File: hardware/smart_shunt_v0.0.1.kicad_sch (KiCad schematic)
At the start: 42 parts, among them J1 SHUNT +, J2 SHUNT -, J3 VIn, J4 USB_C_Receptacle_USB2.0, J5 GND, SW1 SW_Push, SW2 SW_Push, U1 ESP32-C3-MINI-1, U4 INA226, U5 TPS562201

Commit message: v0.0.2 update, before FETs
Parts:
- removed JP1: SolderJumper_2_Open, Jumper:SolderJumper-2_P1.3mm_Open_TrianglePad1.0x1.5mm, symbol Jumper:SolderJumper_2_Open
- removed TP3, TP4, TP5, TP6, TP7, TP8, TP9: TestPoint, TestPoint:TestPoint_Pad_D1.0mm, symbol Connector:TestPoint
- added D5: 1N5819WS, Diode_SMD:D_SOD-323, symbol Diode:1N5819WS
- J1, J2: footprint Acea:MountingHole_10.5mm -> ShuntToPCB:MountingHole_17mm
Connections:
- net SHUNT+: now also C4.1, C6.1, U4.8 (Vbus), U5.3 (VIN), U5.5 (EN), D5.1 (K)
- net USB_VBUS: now also D5.2 (A)
- net LOAD_DISCONNECT: now reaches U1.19 (GPIO5/ADC2_CH0)
- removed net BATTV: C4.1, C6.1, J3.1 (Pin_1), U4.8 (Vbus), U5.3 (VIN), U5.5 (EN)
- no-connect marks 8 -> 7
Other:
- note added: "Counts the current draw from the shunt"
- moved on the sheet: C10, C3, C4, C6, C7, C9, J3, J5, L1, R11, R12, U5

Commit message: v0.0.3 off to JLCPCB
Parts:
- added C11: 100nF, Capacitor_SMD:C_0603_1608Metric, symbol Device:C_Small
- added C12: 220nF, Capacitor_SMD:C_0805_2012Metric, symbol Device:C_Small
- added C13: 220uF 50V, Capacitor_SMD:CP_Elec_8x10.5, symbol Device:C_Polarized_Small
- added J6: SHUNT +, ShuntToPCB:MountingHole_17mm, symbol Connector:Conn_01x01_Socket
- added Q1, Q2: CMSL008N06, CMSL008N06:CMSL008N06, symbol Transistor_FET:STD7NK40Z
- added R13: 33.2k, Resistor_SMD:R_0603_1608Metric, symbol Device:R
- added R14: 180k, Resistor_SMD:R_0603_1608Metric, symbol Device:R
- added U2: LM74502H-Q1, Package_TO_SOT_SMD:SOT-23-8, symbol Sensor_Energy:INA219BxDCN
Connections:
- net GND: now also C11.2, C13.2, R13.2, U2.2 (GND), U2.7 (OV)
- net SHUNT+: now also C11.1, C12.1, C13.1, Q1.2 (D), Q2.2 (D), U2.5 (VS)
- net at U1.6 (GPIO3/ADC1_CH3): now also R13.1, R14.2
- net at J3.1 (Pin_1): now also R14.1
- net LOAD_DISCONNECT renamed LD_DISC
- net LD_DISC: now also U2.1 (EN)
- new net: J6.1 (Pin_1), Q1.3 (S), Q2.3 (S), U2.8 (SRC)
- new net GATE: Q1.1 (G), Q2.1 (G), U2.6 (GATE)
- new net VCAP: C12.2, U2.4 (VCAP)
- no-connect marks 7 -> 6
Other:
- moved on the sheet: C1, C10, C2, C3, C4, C5, C6, C7, C8, C9, D1, D5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

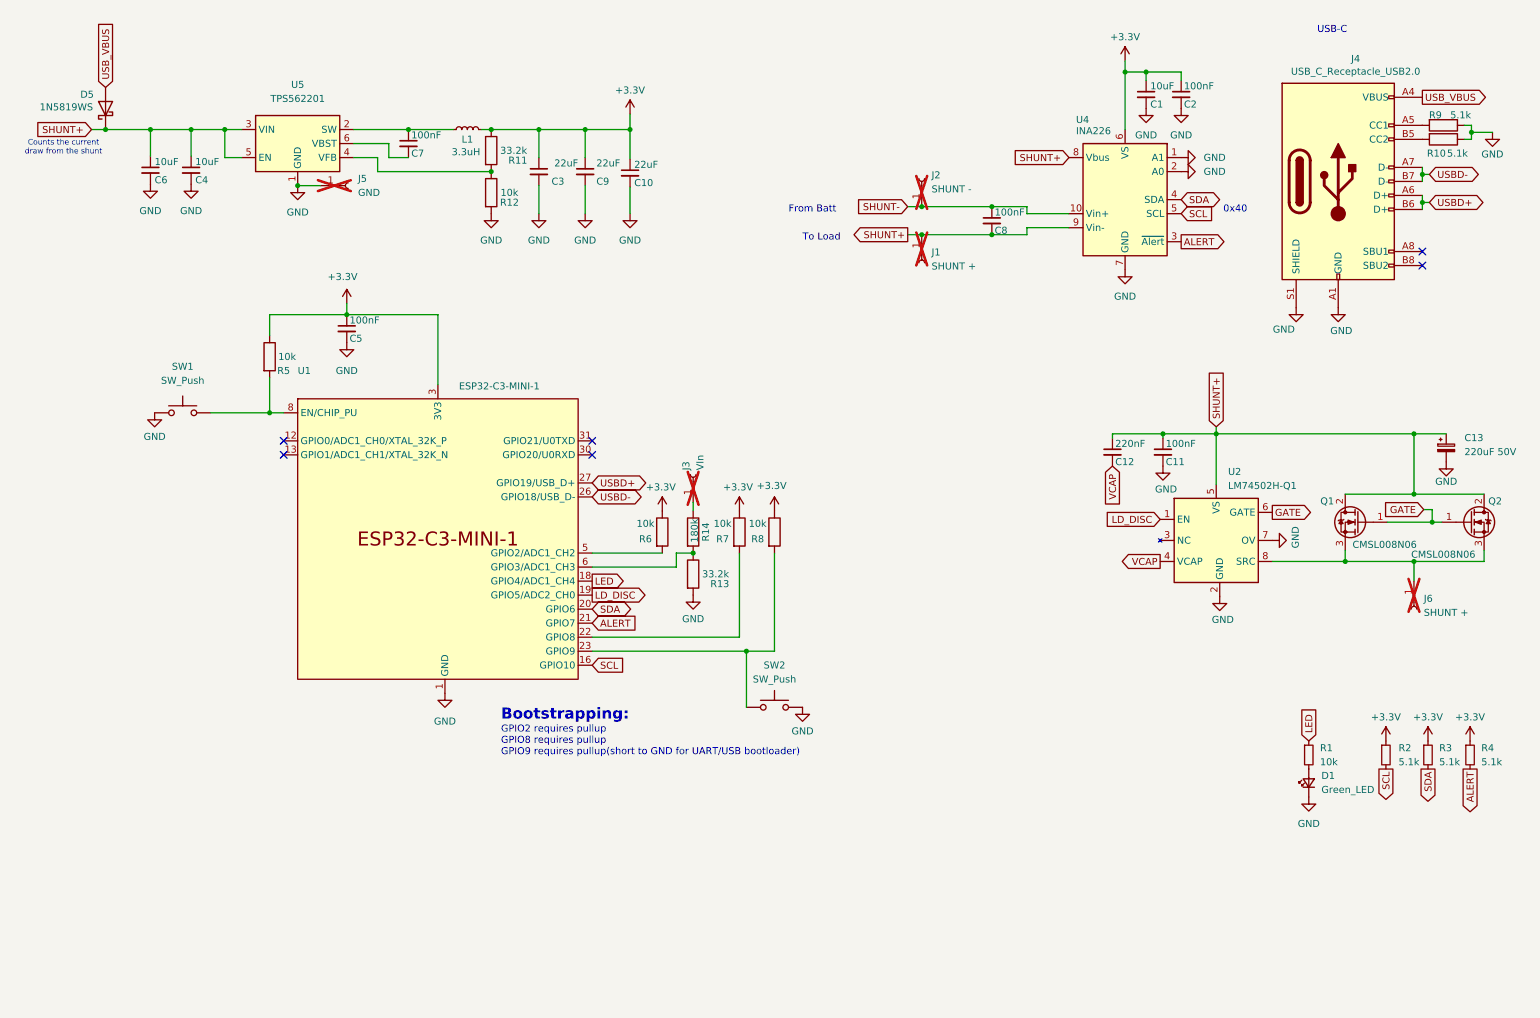
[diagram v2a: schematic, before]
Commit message: Fixing reversed MOSFETs
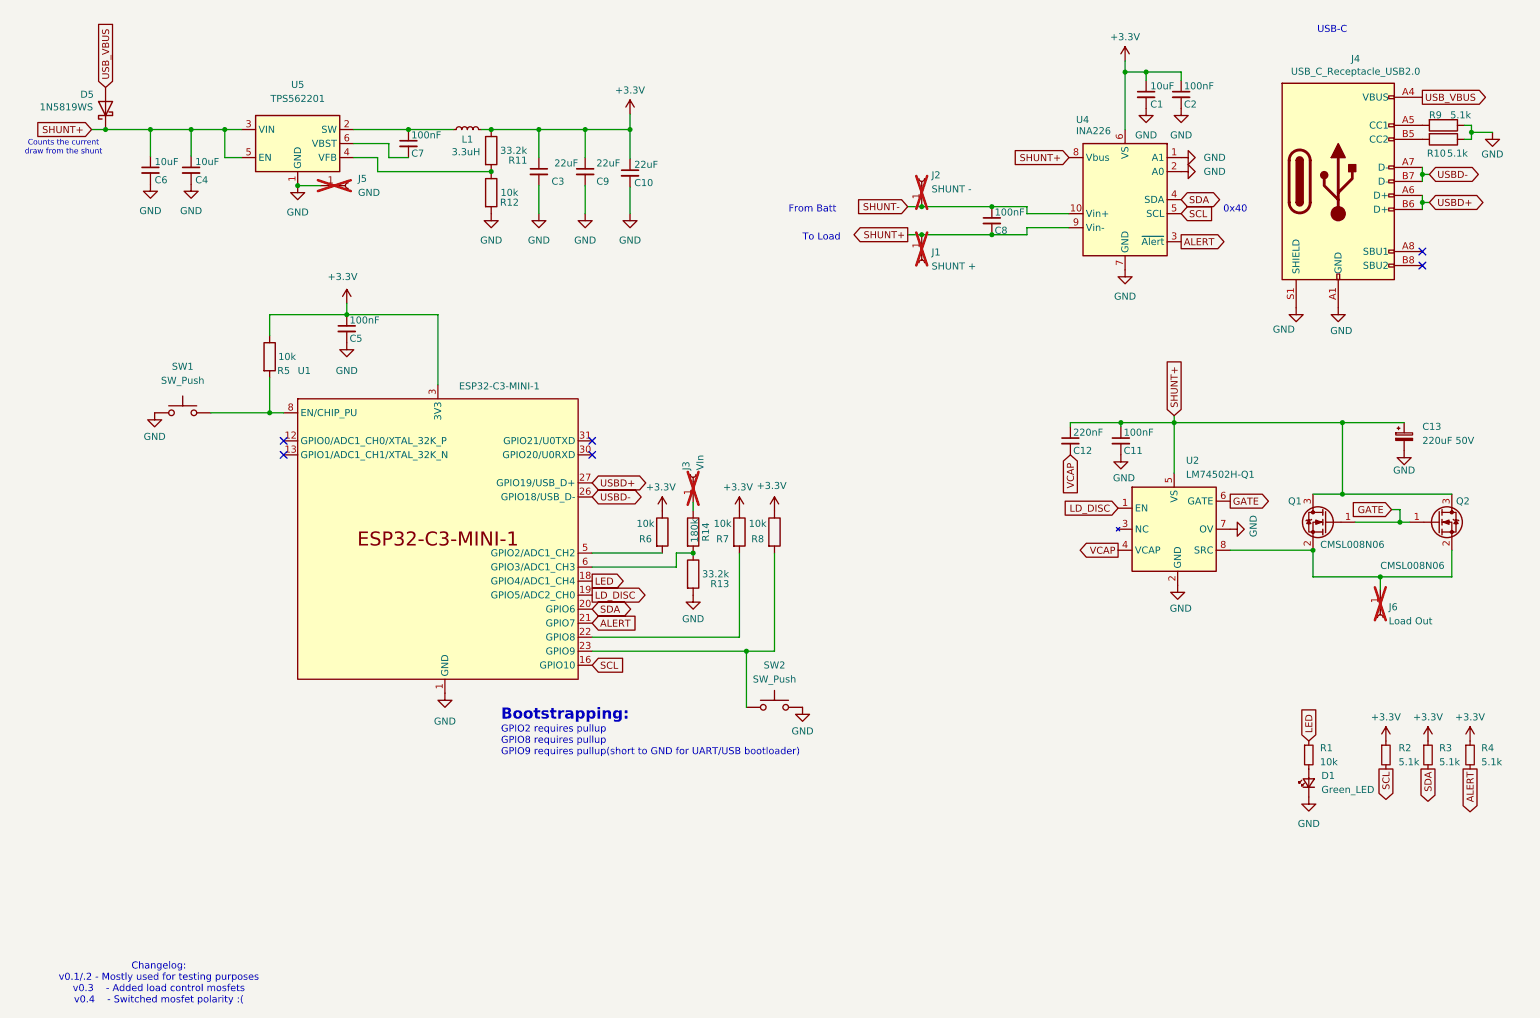
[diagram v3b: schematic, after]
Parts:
- J6: value SHUNT + -> Load Out
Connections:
- net SHUNT+: now also Q1.3 (D), Q2.3 (D); no longer Q1.2 (D), Q2.2 (D)
- net at J6.1 (Pin_1), U2.8 (SRC): now also Q1.2 (S), Q2.2 (S); no longer Q1.3 (S), Q2.3 (S)
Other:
- note added: "Changelog: v0.1/.2 - Mostly used for testing purposes v0.3 - Added load control mosfets v0.4 - Switched mosfet polarity :("
- moved on the sheet: C11, C12, C13, J6, Q1, Q2, U2

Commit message: Sent files to assembler
Removed values from from front fab layer
Added missing reference designators from front fab layer
Added manufacturer and manufacturer part numbers to BOM
Replaced 180K and 220nF parts in BOM
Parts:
- C1: MFR (none) -> Samsung Electro-Mechanics; MFR# (none) -> CL10A106KP8NNNC
- C10, C3, C9: MFR (none) -> Samsung Electro-Mechanics; MFR# (none) -> CL21A226MAQNNNE
- C11, C2, C5, C7, C8: MFR (none) -> YAGEO; MFR# (none) -> CC0603KRX7R9BB104
- C12: MFR (none) -> Samsung Electro-Mechanics; MFR# (none) -> CL21B224KBFNNNE; lcsc (none) -> C5378
- C13: MFR (none) -> Honor Elec; MFR# (none) -> VP1H221M0810
- C4, C6: MFR (none) -> muRata; MFR# (none) -> GRM21BR6YA106KE43L
- D1: MFR (none) -> Yongyu Photoelectric; MFR# (none) -> SZYY0402YG
- D5: MFR (none) -> JSMSEMI; MFR# (none) -> 1N5819WS S4
- J4: MFR (none) -> SHOU HAN; MFR# (none) -> TYPE-C 16P QTWT; lcsc (none) -> C5187472
- L1: MFR (none) -> Sunlord; MFR# (none) -> SWPA4030S3R3MT
- Q1, Q2: MFR (none) -> Cmos; MFR# (none) -> CMSL008N06
- R1, R12, R5, R6, R7, R8: MFR (none) -> UNI-ROYAL; MFR# (none) -> 0603WAF1002T5E
- R10, R2, R3, R4, R9: MFR (none) -> UNI-ROYAL; MFR# (none) -> 0603WAF5101T5E
- R11, R13: MFR (none) -> TyoHM; MFR# (none) -> RMC060333.2K1%N
- R14: MFR (none) -> YAGEO; MFR# (none) -> RC0603FR-07180KL; lcsc (none) -> C123419
- SW1, SW2: MFR (none) -> ALPSALPINE; MFR# (none) -> SKSCLBE010
- U1: MFR (none) -> ESPRESSIF; MFR# (none) -> ESP32-C3-MINI-1-H4
- U2: MFR (none) -> Texas Instruments; MFR# (none) -> TI LM74502HQDDFRQ1
- U4: MFR (none) -> Texas Instruments; MFR# (none) -> INA226AIDGSR
- U5: MFR (none) -> Texas Instruments; MFR# (none) -> TPS562201DDCR
